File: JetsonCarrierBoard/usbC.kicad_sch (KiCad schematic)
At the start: 0 parts

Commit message: Added all USB-C components and started M.2 WiFi
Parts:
- added J?: USB_C_Receptacle, symbol USB_C_Connector:USB_C_Receptacle
- added U?: TPS65987D, symbol PD_controller:TPS65987D
- added U?: TPD6S300A, symbol USB_C_Port_Protector:TPD6S300A
- added U?: HD3SS460, symbol USB_C_Mux:HD3SS460
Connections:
- new net: J?.A1 (GND), J?.A12 (GND), J?.B1 (GND), J?.B12 (GND)
- new net: J?.A4 (VBUS), J?.A9 (VBUS), J?.B4 (VBUS), J?.B9 (VBUS)
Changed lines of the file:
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@@
 (kicad_sch (version 20211123) (generator eeschema)
   (paper "A4")
+  (symbol (lib_id "PD_controller:TPS65987D") (at 128.27 91.44 0) (unit 1)
+    (in_bom yes) (on_board yes) (fields_autoplaced)
+    (property "Reference" "U?" (id 0) (at 128.27 34.451 0))
+    (property "Value" "TPS65987D" (id 1) (at 128.27 36.9879 0))
+    (property "Footprint" "" (id 2) (at 125.73 40.64 0)
+      (effects (font (size 1.27 1.27)) hide)
+    )
+    (property "Datasheet" "https://www.ti.com/lit/ds/symlink/tps65987d.pdf?ts=1662720709173&ref_url=https%253A%252F%252Fwww.ti.com%252Fproduct%252FTPS65987D" (id 3) (at 125.73 40.64 0)
+      (effects (font (size 1.27 1.27)) hide)
+    )
+    (pin "1")
+    (pin "10")
+    (pin "11")
+    (pin "12")
+    (pin "13")
+    (pin "14")
+    (pin "15")
+    (pin "16")
+    (pin "17")
+    (pin "18")
+    (pin "19")
+    (pin "2")
+    (pin "20")
+    (pin "21")
+    (pin "22")
+    (pin "23")
+    (pin "24")
+    (pin "25")
+    (pin "26")
+    (pin "26")
+    (pin "27")
+    (pin "28")
+    (pin "29")
+    (pin "3")
+    (pin "30")
+    (pin "31")
+    (pin "32")
+    (pin "33")
+    (pin "34")
+    (pin "35")
+    (pin "36")
+    (pin "37")
+    (pin "38")
+    (pin "39")
+    (pin "4")
+    (pin "40")
+    (pin "41")
+    (pin "42")
+    (pin "43")
+    (pin "44")
+    (pin "45")
+    (pin "46")
+    (pin "47")
+    (pin "48")
+    (pin "49")
+    (pin "5")
+    (pin "50")
+    (pin "51")
+    (pin "52")
+    (pin "54")
+    (pin "55")
+    (pin "56")
+    (pin "57")
+    (pin "58")
+    (pin "59")
+    (pin "6")
+    (pin "7")
+    (pin "8")
+    (pin "9")
+  )
+  (symbol (lib_id "USB_C_Port_Protector:TPD6S300A") (at 241.3 64.77 0) (unit 1)
+    (in_bom yes) (on_board yes) (fields_autoplaced)
+    (property "Reference" "U?" (id 0) (at 243.205 112.4696 0))
+    (property "Value" "TPD6S300A" (id 1) (at 243.205 115.0065 0))
+    (property "Footprint" "" (id 2) (at 241.3 71.12 0)
+      (effects (font (size 1.27 1.27)) hide)
+    )
+    (property "Datasheet" "" (id 3) (at 241.3 71.12 0)
+      (effects (font (size 1.27 1.27)) hide)
+    )
+    (pin "1")
+    (pin "10")
+    (pin "11")
+    (pin "12")
+    (pin "13")
+    (pin "14")
+    (pin "15")
+    (pin "16")
+    (pin "17")
+    (pin "18")
+    (pin "19")
+    (pin "2")
+    (pin "20")
+    (pin "21")
+    (pin "3")
+    (pin "4")
+    (pin "5")
+    (pin "6")
+    (pin "7")
+    (pin "8")
+    (pin "9")
+  )
+  (symbol (lib_id "USB_C_Connector:USB_C_Receptacle") (at 176.53 74.93 0) (unit 1)
+    (in_bom yes) (on_board yes) (fields_autoplaced)
+    (property "Reference" "J?" (id 0) (at 176.53 43.2902 0))
+    (property "Value" "USB_C_Receptacle" (id 1) (at 176.53 45.8271 0))
+    (property "Footprint" "" (id 2) (at 180.34 74.93 0)
+      (effects (font (size 1.27 1.27)) hide)
+    )
+    (property "Datasheet" "https://www.usb.org/sites/default/files/documents/usb_type-c.zip" (id 3) (at 180.594 74.676 0)
+      (effects (font (size 1.27 1.27)) hide)
+    )
+    (pin "A1")
+    (pin "A10")
+    (pin "A11")
+    (pin "A12")
+    (pin "A2")
+    (pin "A3")
+    (pin "A4")
+    (pin "A5")
+    (pin "A6")
+    (pin "A7")
+    (pin "A8")
+    (pin "A9")
+    (pin "B1")
+    (pin "B10")
+    (pin "B11")
+    (pin "B12")
+    (pin "B2")
+    (pin "B3")
+    (pin "B4")
+    (pin "B5")
+    (pin "B6")
+    (pin "B7")
+    (pin "B8")
+    (pin "B9")
+    (pin "S1")
+  )
+  (symbol (lib_id "USB_C_Mux:HD3SS460") (at 74.93 78.74 0) (unit 1)
+    (in_bom yes) (on_board yes) (fields_autoplaced)
+    (property "Reference" "U?" (id 0) (at 76.9494 50.961 0)
+      (effects (font (size 1.27 1.27)) (justify left))
+    )
+    (property "Value" "HD3SS460" (id 1) (at 76.9494 53.4979 0)
+      (effects (font (size 1.27 1.27)) (justify left))
+    )
+    (property "Footprint" "" (id 2) (at 75.311 78.4352 0)
+      (effects (font (size 1.27 1.27)) hide)
+    )
+    (property "Datasheet" "https://www.ti.com/lit/ds/symlink/hd3ss460.pdf?ts=1662747973822&ref_url=https%253A%252F%252Fwww.ti.com%252Fproduct%252FHD3SS460%253FHQS%253Dti-null-null-verifimanuf_df-manu-pf-octopart-wwe" (id 3) (at 75.311 78.4352 0)
+      (effects (font (size 1.27 1.27)) hide)
+    )
+    (pin "0")
+    (pin "1")
+    (pin "10")
+    (pin "11")
+    (pin "12")
+    (pin "13")
+    (pin "14")
+    (pin "15")
+    (pin "16")
+    (pin "17")
+    (pin "18")
+    (pin "19")
+    (pin "2")
+    (pin "20")
+    (pin "21")
+    (pin "22")
+    (pin "23")
+    (pin "24")
+    (pin "25")
+    (pin "26")
+    (pin "27")
+    (pin "28")
+    (pin "3")
+    (pin "4")
+    (pin "5")
+    (pin "6")
+    (pin "7")
+    (pin "8")
+    (pin "9")
+  )
 )

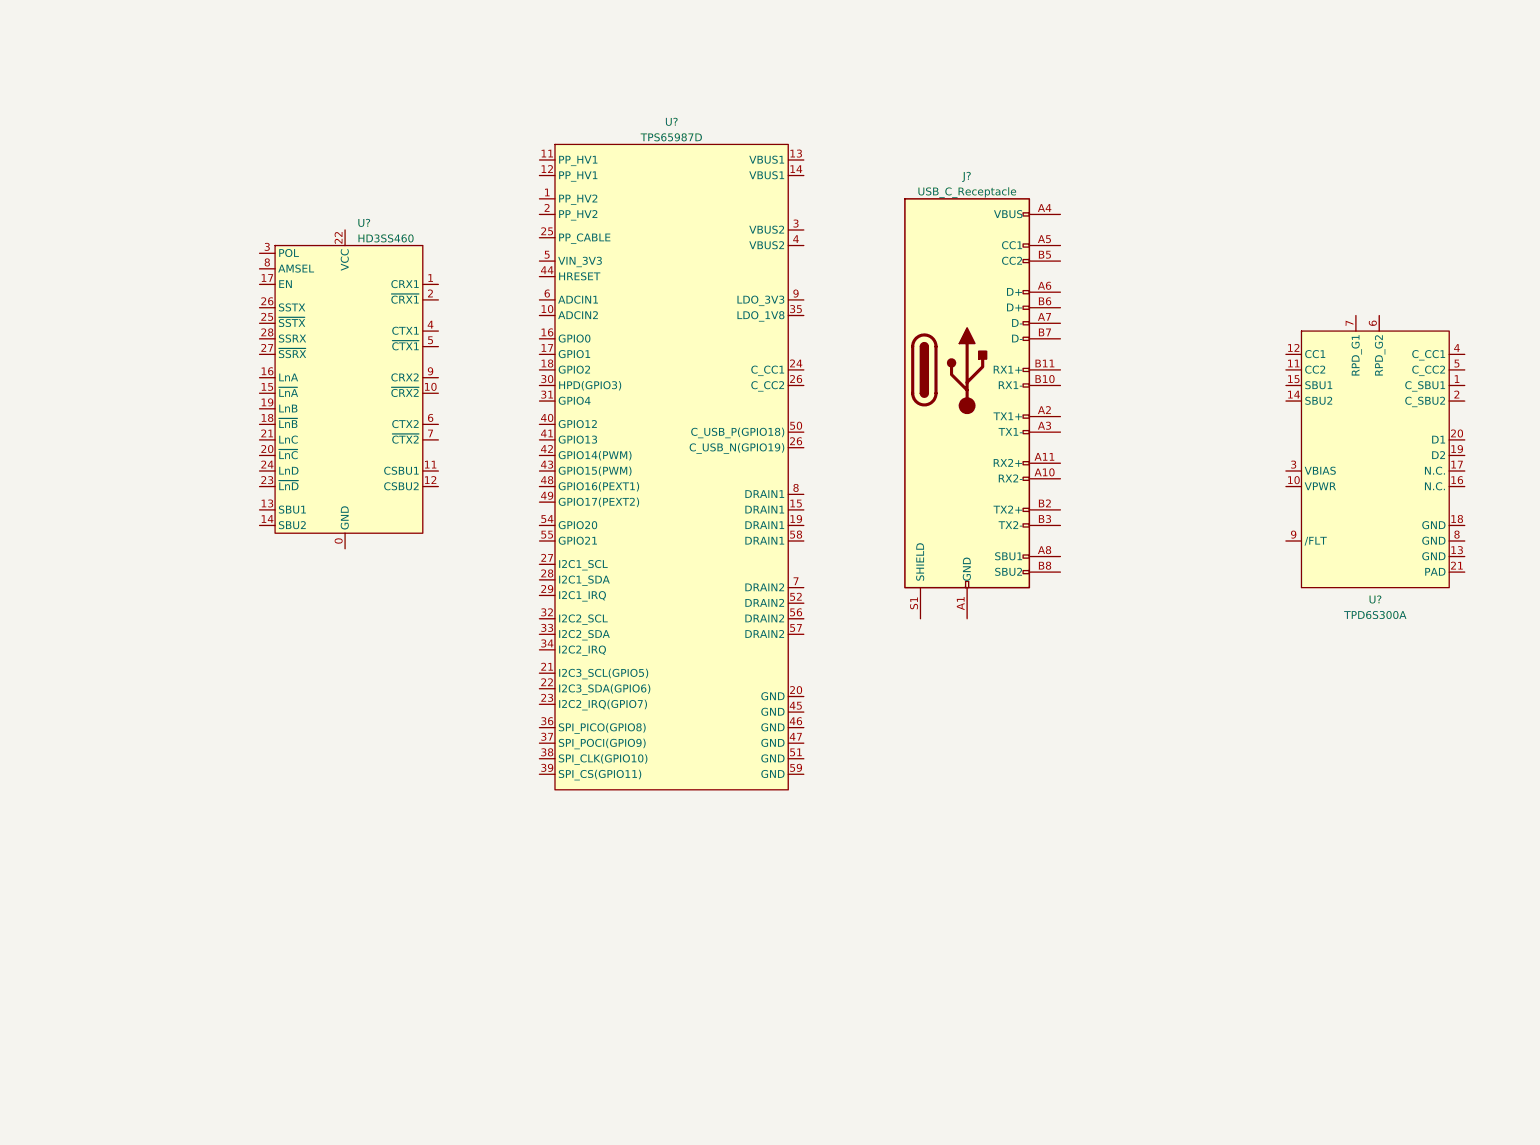
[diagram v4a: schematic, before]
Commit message: USB C System Power assignments
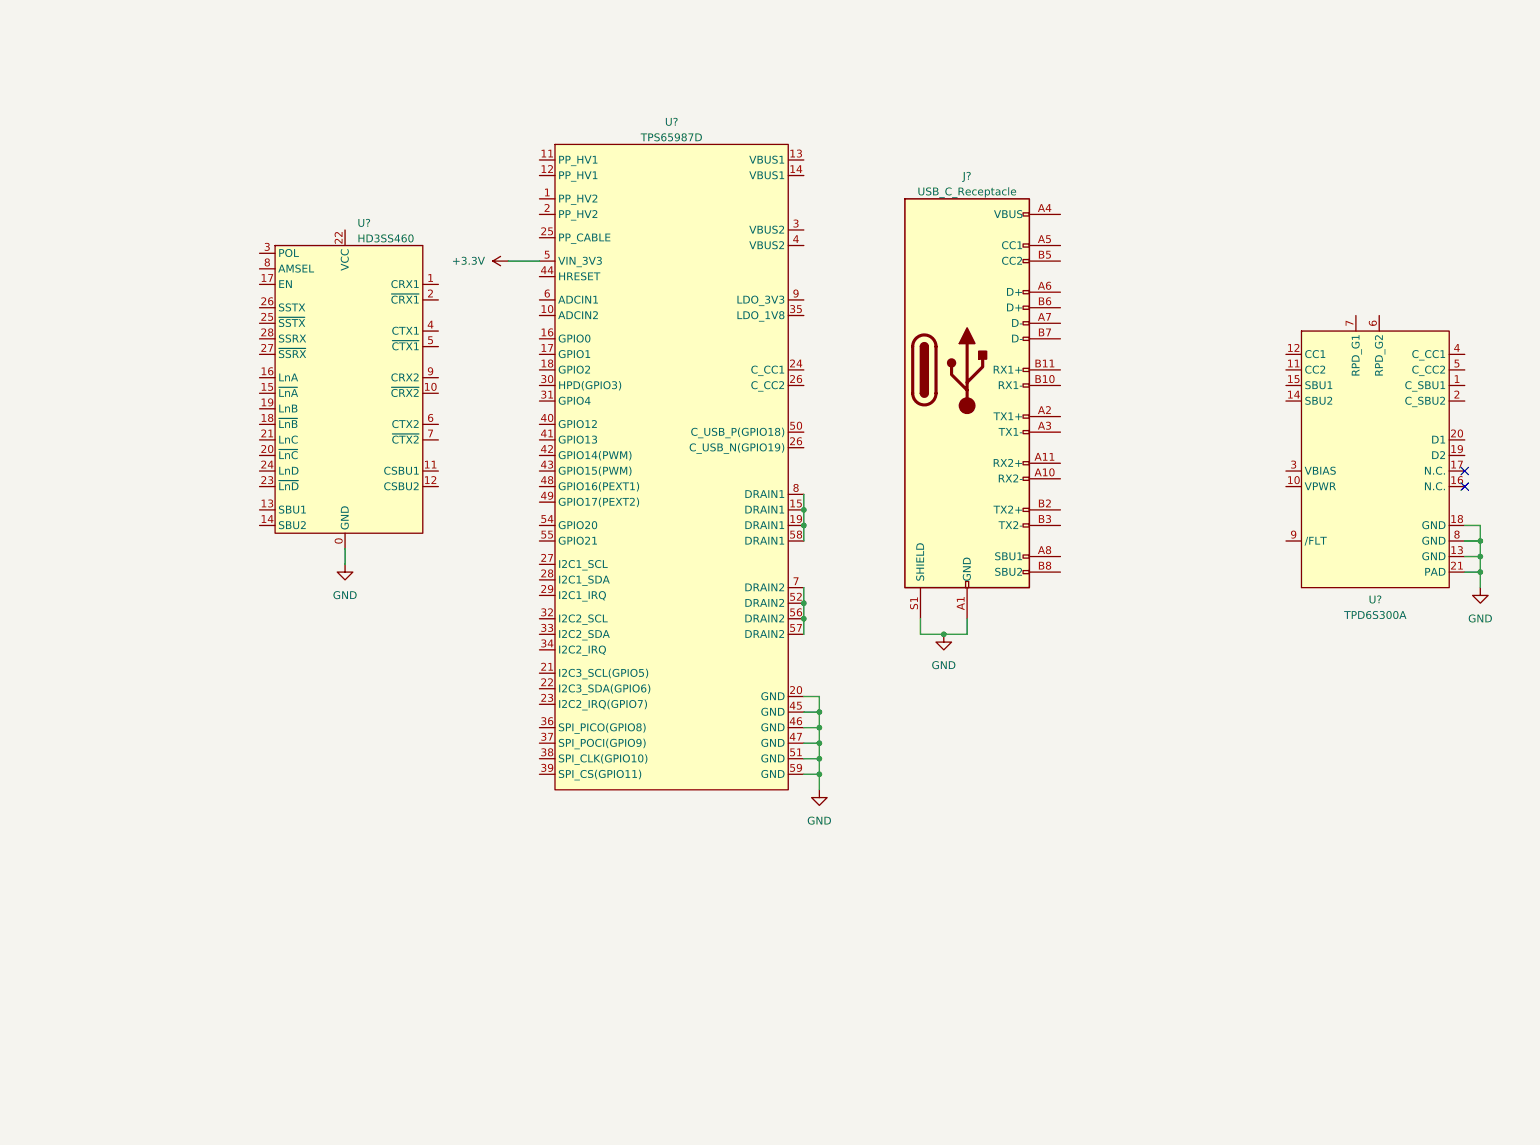
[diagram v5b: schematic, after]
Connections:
- net at U?.15 (DRAIN1): now also U?.19 (DRAIN1), U?.58 (DRAIN1), U?.8 (DRAIN1)
- net GND: now reaches U?.20 (GND)
- net GND: now also J?.A1 (GND), J?.A12 (GND), J?.B1 (GND), J?.B12 (GND), J?.S1 (SHIELD), U?.0 (GND), U?.13 (GND), U?.18 (GND), U?.21 (PAD), U?.45 (GND), U?.46 (GND), U?.47 (GND), U?.51 (GND), U?.59 (GND), U?.8 (GND)
- net +3.3V: now reaches U?.5 (VIN_3V3)
- net at U?.52 (DRAIN2): now also U?.56 (DRAIN2), U?.57 (DRAIN2), U?.7 (DRAIN2)
- no-connect marks 0 -> 2
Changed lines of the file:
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@@
 (kicad_sch (version 20211123) (generator eeschema)
   (paper "A4")
+  (junction (at 172.72 118.11) (diameter 0) (color 0 0 0 0)
+  )
+  (junction (at 149.86 100.33) (diameter 0) (color 0 0 0 0)
+  )
+  (junction (at 260.35 102.87) (diameter 0) (color 0 0 0 0)
+  )
+  (junction (at 152.4 133.35) (diameter 0) (color 0 0 0 0)
+  )
+  (junction (at 152.4 130.81) (diameter 0) (color 0 0 0 0)
+  )
+  (junction (at 260.35 107.95) (diameter 0) (color 0 0 0 0)
+  )
+  (junction (at 149.86 113.03) (diameter 0) (color 0 0 0 0)
+  )
+  (junction (at 149.86 115.57) (diameter 0) (color 0 0 0 0)
+  )
+  (junction (at 149.86 97.79) (diameter 0) (color 0 0 0 0)
+  )
+  (junction (at 152.4 140.97) (diameter 0) (color 0 0 0 0)
+  )
+  (junction (at 260.35 105.41) (diameter 0) (color 0 0 0 0)
+  )
+  (junction (at 152.4 138.43) (diameter 0) (color 0 0 0 0)
+  )
+  (junction (at 152.4 135.89) (diameter 0) (color 0 0 0 0)
+  )
+  (no_connect (at 257.81 93.98))
+  (no_connect (at 257.81 91.44))
+  (wire (pts (xy 152.4 135.89) (xy 152.4 133.35))
+    (stroke (width 0) (type default) (color 0 0 0 0))
+  )
+  (wire (pts (xy 152.4 138.43) (xy 149.86 138.43))
+    (stroke (width 0) (type default) (color 0 0 0 0))
+  )
+  (wire (pts (xy 260.35 105.41) (xy 260.35 107.95))
+    (stroke (width 0) (type default) (color 0 0 0 0))
+  )
+  (wire (pts (xy 149.86 95.25) (xy 149.86 97.79))
+    (stroke (width 0) (type default) (color 0 0 0 0))
+  )
+  (wire (pts (xy 152.4 140.97) (xy 152.4 138.43))
+    (stroke (width 0) (type default) (color 0 0 0 0))
+  )
+  (wire (pts (xy 152.4 130.81) (xy 152.4 128.27))
+    (stroke (width 0) (type default) (color 0 0 0 0))
+  )
+  (wire (pts (xy 260.35 110.49) (xy 260.35 107.95))
+    (stroke (width 0) (type default) (color 0 0 0 0))
+  )
+  (wire (pts (xy 257.81 100.33) (xy 260.35 100.33))
+    (stroke (width 0) (type default) (color 0 0 0 0))
+  )
+  (wire (pts (xy 149.86 97.79) (xy 149.86 100.33))
+    (stroke (width 0) (type default) (color 0 0 0 0))
+  )
+  (wire (pts (xy 149.86 113.03) (xy 149.86 115.57))
+    (stroke (width 0) (type default) (color 0 0 0 0))
+  )
+  (wire (pts (xy 260.35 102.87) (xy 260.35 105.41))
+    (stroke (width 0) (type default) (color 0 0 0 0))
+  )
+  (wire (pts (xy 168.91 115.57) (xy 168.91 118.11))
+    (stroke (width 0) (type default) (color 0 0 0 0))
+  )
+  (wire (pts (xy 152.4 135.89) (xy 149.86 135.89))
+    (stroke (width 0) (type default) (color 0 0 0 0))
+  )
+  (wire (pts (xy 176.53 118.11) (xy 176.53 115.57))
+    (stroke (width 0) (type default) (color 0 0 0 0))
+  )
+  (wire (pts (xy 172.72 118.11) (xy 176.53 118.11))
+    (stroke (width 0) (type default) (color 0 0 0 0))
+  )
+  (wire (pts (xy 152.4 130.81) (xy 149.86 130.81))
+    (stroke (width 0) (type default) (color 0 0 0 0))
+  )
+  (wire (pts (xy 149.86 100.33) (xy 149.86 102.87))
+    (stroke (width 0) (type default) (color 0 0 0 0))
+  )
+  (wire (pts (xy 257.81 105.41) (xy 260.35 105.41))
+    (stroke (width 0) (type default) (color 0 0 0 0))
+  )
+  (wire (pts (xy 152.4 138.43) (xy 152.4 135.89))
+    (stroke (width 0) (type default) (color 0 0 0 0))
+  )
+  (wire (pts (xy 168.91 118.11) (xy 172.72 118.11))
+    (stroke (width 0) (type default) (color 0 0 0 0))
+  )
+  (wire (pts (xy 257.81 102.87) (xy 260.35 102.87))
+    (stroke (width 0) (type default) (color 0 0 0 0))
+  )
+  (wire (pts (xy 152.4 128.27) (xy 149.86 128.27))
+    (stroke (width 0) (type default) (color 0 0 0 0))
+  )
+  (wire (pts (xy 260.35 100.33) (xy 260.35 102.87))
+    (stroke (width 0) (type default) (color 0 0 0 0))
+  )
+  (wire (pts (xy 260.35 107.95) (xy 257.81 107.95))
+    (stroke (width 0) (type default) (color 0 0 0 0))
+  )
+  (wire (pts (xy 152.4 143.51) (xy 152.4 140.97))
+    (stroke (width 0) (type default) (color 0 0 0 0))
+  )
+  (wire (pts (xy 152.4 133.35) (xy 152.4 130.81))
+    (stroke (width 0) (type default) (color 0 0 0 0))
+  )
+  (wire (pts (xy 152.4 140.97) (xy 149.86 140.97))
+    (stroke (width 0) (type default) (color 0 0 0 0))
+  )
+  (wire (pts (xy 74.93 104.14) (xy 74.93 106.68))
+    (stroke (width 0) (type default) (color 0 0 0 0))
+  )
+  (wire (pts (xy 101.6 57.15) (xy 106.68 57.15))
+    (stroke (width 0) (type default) (color 0 0 0 0))
+  )
+  (wire (pts (xy 149.86 133.35) (xy 152.4 133.35))
+    (stroke (width 0) (type default) (color 0 0 0 0))
+  )
+  (wire (pts (xy 149.86 110.49) (xy 149.86 113.03))
+    (stroke (width 0) (type default) (color 0 0 0 0))
+  )
+  (wire (pts (xy 149.86 115.57) (xy 149.86 118.11))
+    (stroke (width 0) (type default) (color 0 0 0 0))
+  )
   (symbol (lib_id "PD_controller:TPS65987D") (at 128.27 91.44 0) (unit 1)
     (in_bom yes) (on_board yes) (fields_autoplaced)
@@
     (pin "9")
   )
+  (symbol (lib_id "power:+3.3V") (at 101.6 57.15 90) (unit 1)
+    (in_bom yes) (on_board yes) (fields_autoplaced)
+    (property "Reference" "#PWR?" (id 0) (at 105.41 57.15 0)
+      (effects (font (size 1.27 1.27)) hide)
+    )
+    (property "Value" "+3.3V" (id 1) (at 97.79 57.1499 90)
+      (effects (font (size 1.27 1.27)) (justify left))
+    )
+    (property "Footprint" "" (id 2) (at 101.6 57.15 0)
+      (effects (font (size 1.27 1.27)) hide)
+    )
+    (property "Datasheet" "" (id 3) (at 101.6 57.15 0)
+      (effects (font (size 1.27 1.27)) hide)
+    )
+    (pin "1")
+  )
   (symbol (lib_id "USB_C_Port_Protector:TPD6S300A") (at 241.3 64.77 0) (unit 1)
     (in_bom yes) (on_board yes) (fields_autoplaced)
@@
     (pin "B9")
     (pin "S1")
+  )
+  (symbol (lib_id "power:GND") (at 74.93 106.68 0) (unit 1)
+    (in_bom yes) (on_board yes) (fields_autoplaced)
+    (property "Reference" "#PWR?" (id 0) (at 74.93 113.03 0)
+      (effects (font (size 1.27 1.27)) hide)
+    )
+    (property "Value" "GND" (id 1) (at 74.93 111.76 0))
+    (property "Footprint" "" (id 2) (at 74.93 106.68 0)
+      (effects (font (size 1.27 1.27)) hide)
+    )
+    (property "Datasheet" "" (id 3) (at 74.93 106.68 0)
+      (effects (font (size 1.27 1.27)) hide)
+    )
+    (pin "1")
+  )
+  (symbol (lib_id "power:GND") (at 152.4 143.51 0) (unit 1)
+    (in_bom yes) (on_board yes) (fields_autoplaced)
+    (property "Reference" "#PWR?" (id 0) (at 152.4 149.86 0)
+      (effects (font (size 1.27 1.27)) hide)
+    )
+    (property "Value" "GND" (id 1) (at 152.4 148.59 0))
+    (property "Footprint" "" (id 2) (at 152.4 143.51 0)
+      (effects (font (size 1.27 1.27)) hide)
+    )
+    (property "Datasheet" "" (id 3) (at 152.4 143.51 0)
+      (effects (font (size 1.27 1.27)) hide)
+    )
+    (pin "1")
   )
   (symbol (lib_id "USB_C_Mux:HD3SS460") (at 74.93 78.74 0) (unit 1)
@@
     (pin "9")
   )
+  (symbol (lib_id "power:GND") (at 260.35 110.49 0) (unit 1)
+    (in_bom yes) (on_board yes) (fields_autoplaced)
+    (property "Reference" "#PWR?" (id 0) (at 260.35 116.84 0)
+      (effects (font (size 1.27 1.27)) hide)
+    )
+    (property "Value" "GND" (id 1) (at 260.35 115.57 0))
+    (property "Footprint" "" (id 2) (at 260.35 110.49 0)
+      (effects (font (size 1.27 1.27)) hide)
+    )
+    (property "Datasheet" "" (id 3) (at 260.35 110.49 0)
+      (effects (font (size 1.27 1.27)) hide)
+    )
+    (pin "1")
+  )
+  (symbol (lib_id "power:GND") (at 172.72 118.11 0) (unit 1)
+    (in_bom yes) (on_board yes) (fields_autoplaced)
+    (property "Reference" "#PWR?" (id 0) (at 172.72 124.46 0)
+      (effects (font (size 1.27 1.27)) hide)
+    )
+    (property "Value" "GND" (id 1) (at 172.72 123.19 0))
+    (property "Footprint" "" (id 2) (at 172.72 118.11 0)
+      (effects (font (size 1.27 1.27)) hide)
+    )
+    (property "Datasheet" "" (id 3) (at 172.72 118.11 0)
+      (effects (font (size 1.27 1.27)) hide)
+    )
+    (pin "1")
+  )
 )
